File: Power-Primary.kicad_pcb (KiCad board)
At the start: 2 copper layers, 174 x 72 mm, 53 parts, among them J1 HV in, J10 SPARE, J11 SPARE, J2 Dashboard, J3 Telemetry, J4 Motor, J5 MPPT 1, J6 MPPT 2, J7 BPS, J8 Primary Disconn., J9 SPARE, U1 Mean_Well_12V

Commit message: finished PCB waiting for edits
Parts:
- added D11: LED, LED_THT:LED_D3.0mm, F.Cu at (200.7, 100.3)
- added D12: LED, LED_THT:LED_D3.0mm, F.Cu at (215.9, 100.3)
- added D13: LED, LED_THT:LED_D3.0mm, F.Cu at (231.1, 100.3)
- added D14: LED, LED_THT:LED_D3.0mm, F.Cu at (231.1, 87.6)
- added D15: LED, LED_THT:LED_D3.0mm, F.Cu at (215.9, 87.6)
- added D16: LED, LED_THT:LED_D3.0mm, F.Cu at (200.7, 87.6)
- added F12: SPARE, Fuse:Fuseholder_Blade_Mini_Keystone_3568, F.Cu at (195.2, 100.6)
- added F13: SPARE, Fuse:Fuseholder_Blade_Mini_Keystone_3568, F.Cu at (210.4, 100.6)
- added F14: SPARE, Fuse:Fuseholder_Blade_Mini_Keystone_3568, F.Cu at (225.7, 100.6)
- added F15: SPARE, Fuse:Fuseholder_Blade_Mini_Keystone_3568, F.Cu at (222.2, 87.4)
- added F16: SPARE, Fuse:Fuseholder_Blade_Mini_Keystone_3568, F.Cu at (207.0, 87.4)
- added F17: SPARE, Fuse:Fuseholder_Blade_Mini_Keystone_3568, F.Cu at (191.8, 87.4)
- added J12: SPARE, Connector_Molex:Molex_Micro-Fit_3.0_43650-0215_1x02_P3.00mm_Vertical, F.Cu at (191.8, 118.1)
- added J13: SPARE, Connector_Molex:Molex_Micro-Fit_3.0_43650-0215_1x02_P3.00mm_Vertical, F.Cu at (207.0, 118.1)
- added J14: SPARE, Connector_Molex:Molex_Micro-Fit_3.0_43650-0215_1x02_P3.00mm_Vertical, F.Cu at (222.2, 118.1)
- added J15: SPARE, Connector_Molex:Molex_Micro-Fit_3.0_43650-0215_1x02_P3.00mm_Vertical, F.Cu at (225.8, 66.0)
- added J16: SPARE, Connector_Molex:Molex_Micro-Fit_3.0_43650-0215_1x02_P3.00mm_Vertical, F.Cu at (210.5, 66.0)
- added J17: SPARE, Connector_Molex:Molex_Micro-Fit_3.0_43650-0215_1x02_P3.00mm_Vertical, F.Cu at (195.3, 66.0)
- added R11: 11K, Resistor_THT:R_Axial_DIN0204_L3.6mm_D1.6mm_P7.62mm_Horizontal, F.Cu at (200.7, 110.5)
- added R12: 11K, Resistor_THT:R_Axial_DIN0204_L3.6mm_D1.6mm_P7.62mm_Horizontal, F.Cu at (215.9, 110.5)
- added R13: 11K, Resistor_THT:R_Axial_DIN0204_L3.6mm_D1.6mm_P7.62mm_Horizontal, F.Cu at (231.1, 110.5)
- added R14: 11K, Resistor_THT:R_Axial_DIN0204_L3.6mm_D1.6mm_P7.62mm_Horizontal, F.Cu at (231.1, 77.5)
- added R15: 11K, Resistor_THT:R_Axial_DIN0204_L3.6mm_D1.6mm_P7.62mm_Horizontal, F.Cu at (215.9, 77.5)
- added R16: 11K, Resistor_THT:R_Axial_DIN0204_L3.6mm_D1.6mm_P7.62mm_Horizontal, F.Cu at (200.7, 77.5)
- moved D9 35.6 mm to (113.6, 89.6)
- moved F3 35.6 mm to (108.3, 100.7)
- moved F4 35.6 mm to (122.8, 100.7)
- moved J1 35.6 mm to (58.5, 94.9)
- moved D17 35.6 mm to (173.8, 74.4)
- moved D3 35.6 mm to (128.2, 97.8)
- moved D4 35.6 mm to (143.1, 97.8)
- moved D5 35.6 mm to (158.1, 97.8)
- moved D6 35.6 mm to (158.2, 89.6)
- moved D7 35.6 mm to (143.1, 89.6)
- moved D8 35.6 mm to (128.2, 89.6)
- moved F10 35.6 mm to (104.9, 86.8)
- moved F5 35.6 mm to (137.6, 100.7)
- moved F6 35.6 mm to (152.4, 100.7)
- moved F7 35.6 mm to (149.0, 86.8)
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- renumbered D11 to D17, R11 to R18
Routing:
- net Net-(F16-Pad2): track 0.00 -> 25.8 mm, vias 0 -> 1
- net Net-(F17-Pad2): track 0.00 -> 25.8 mm, vias 0 -> 1
- net Net-(F15-Pad2): track 0.00 -> 25.7 mm, vias 0 -> 1
- net Net-(F14-Pad2): track 0.00 -> 21.6 mm, vias 0 -> 1
- net Net-(F13-Pad2): track 0.00 -> 21.6 mm, vias 0 -> 1
- net Net-(F12-Pad2): track 0.00 -> 21.6 mm, vias 0 -> 1
- net Net-(D13-Pad2): track 0.00 -> 2.54 mm
- net Net-(D12-Pad2): track 0.00 -> 2.54 mm
- net Net-(D11-Pad2): track 0.00 -> 2.54 mm
- net Net-(D16-Pad2): track 0.00 -> 2.54 mm
- net Net-(D15-Pad2): track 0.00 -> 2.54 mm
- net Net-(D14-Pad2): track 0.00 -> 2.54 mm
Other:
- board size 174 x 72 mm -> 226.1 x 72.4 mm

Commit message: pcb edits
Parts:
- moved REF** 1.27 mm to (236.2, 123.2)
- moved F15 0.62 mm to (222.2, 86.8)
- moved F16 0.62 mm to (207.0, 86.8)
- moved F17 0.62 mm to (191.8, 86.8)
- moved D14 0.53 mm to (231.1, 87.1)
- moved D15 0.53 mm to (215.9, 87.1)
- moved D16 0.53 mm to (200.7, 87.1)
- moved R14 0.51 mm to (231.1, 77.0)
- moved R15 0.51 mm to (215.9, 77.0)
- moved R16 0.51 mm to (200.7, 77.0)
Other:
- outline, holes or cut-outs redrawn
- board text added: "UTSVT - Power Primary Power Board v1.1 Fall 2020"
- board text removed: "BeVolt PDB Fall 2018 Alex T. Rodriguez James Corbin II"

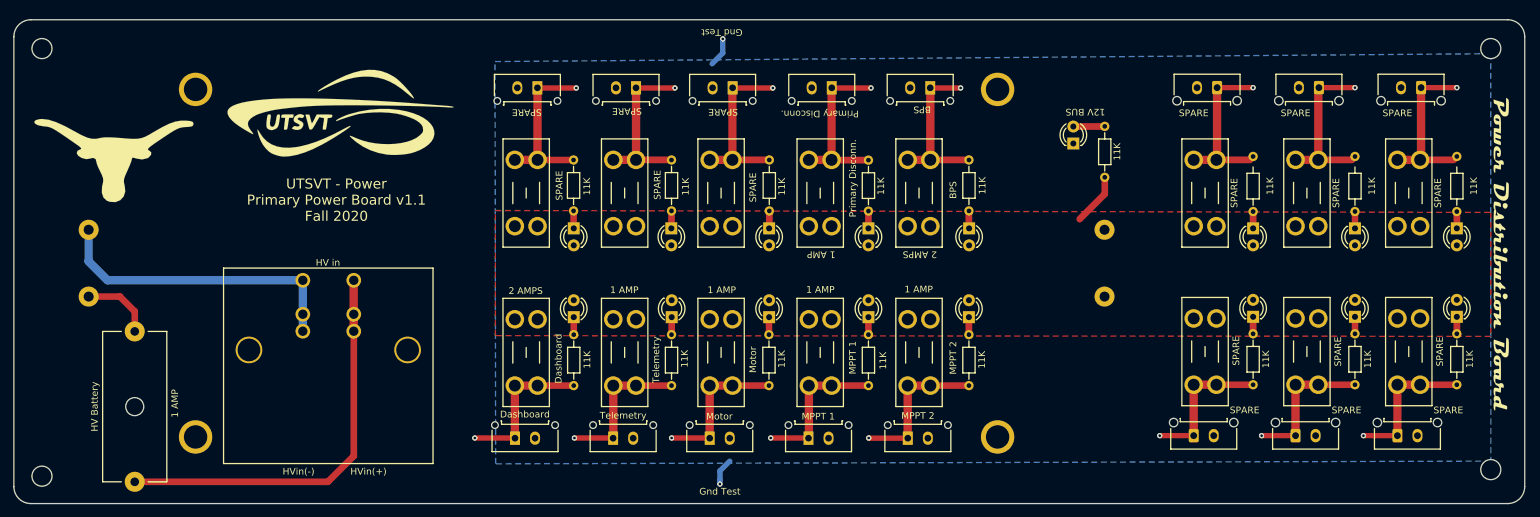
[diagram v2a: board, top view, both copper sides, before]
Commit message: fixed component spacing
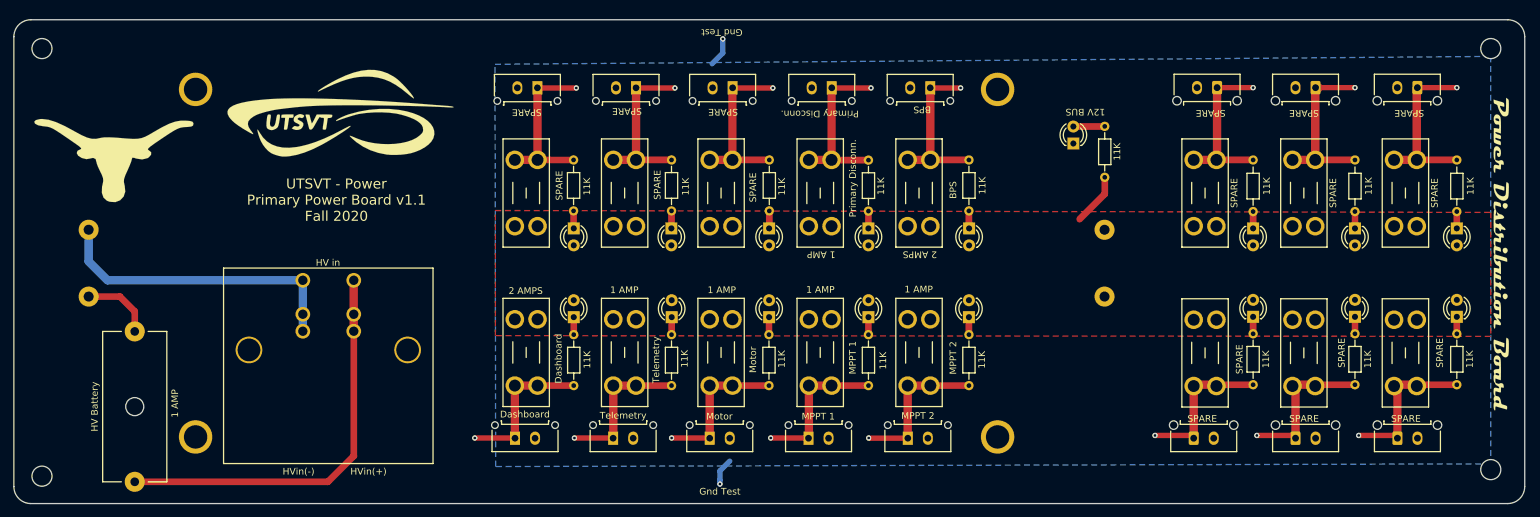
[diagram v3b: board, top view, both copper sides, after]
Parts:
- moved J15 0.56 mm to (225.2, 66.0)
- moved F14 0.54 mm to (225.2, 100.8)
- moved J16 0.51 mm to (210.0, 66.0)
- moved F15 0.50 mm to (221.8, 86.8)
- moved F13 0.50 mm to (210.0, 100.8)
- moved F16 0.46 mm to (206.6, 86.8)
- moved J12 0.38 mm to (191.8, 118.5)
- moved J13 0.38 mm to (207.0, 118.5)
- moved J14 0.38 mm to (222.2, 118.5)
- moved F12 0.20 mm to (195.2, 100.8)
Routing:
- net Net-(F15-Pad2): track 25.5 -> 26.3 mm
- net Net-(F13-Pad2): track 21.6 -> 22.3 mm
- net Net-(F14-Pad2): track 21.6 -> 22.3 mm
- net Net-(F12-Pad2): track 21.6 -> 22.3 mm
